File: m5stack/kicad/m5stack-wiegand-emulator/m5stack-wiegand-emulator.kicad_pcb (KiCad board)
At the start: 2 copper layers, 50 x 50 mm, 59 parts, among them J1 2x15 socket header, J2 2x15 pin header, J3 1x5 female, T1 TestPoint, T2 TestPoint, T3 TestPoint, T4 TestPoint, U1 RP2040, U2 ISOW7841, U3 SN74LVC2G126-EP, U5 SN74AHCT1G125, U6 FISM 1769405241

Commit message: M5: added solder jumpers for TC/RX
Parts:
- added JP4: Jumper:SolderJumper_2_Open, Jumper:SolderJumper-2_P1.3mm_Open_RoundedPad1.0x1.5mm, B.Cu at (114.9, 74.2)
- added JP5: Jumper:SolderJumper_2_Open, Jumper:SolderJumper-2_P1.3mm_Open_RoundedPad1.0x1.5mm, B.Cu at (114.9, 77.7)
- added JP8: Jumper:SolderJumper_2_Open, Jumper:SolderJumper-2_P1.3mm_Open_RoundedPad1.0x1.5mm, B.Cu at (114.9, 81.3)
- added JP9: Jumper:SolderJumper_2_Open, Jumper:SolderJumper-2_P1.3mm_Open_RoundedPad1.0x1.5mm, B.Cu at (114.9, 84.8)
- moved R14 47.1 mm to (108.0, 73.7)
- moved R15 47.1 mm to (108.0, 77.5)
- moved R16 47.1 mm to (108.0, 81.3)
- moved R19 47.1 mm to (108.0, 85.1)
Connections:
- R1 pad 2: /RXD2 -> Net-(JP8-B)
- R17 pad 2: /RXD1 -> Net-(JP4-B)
- R18 pad 2: /TXD1 -> Net-(JP5-B)
- R2 pad 2: /TXD2 -> Net-(JP9-B)
- U1 pad 18: /TXD2 -> Net-(JP9-B)
- U1 pad 19: /RXD2 -> Net-(JP8-B)
- U1 pad 22: /TXD1 -> Net-(JP5-B)
- U1 pad 23: /RXD1 -> Net-(JP4-B)

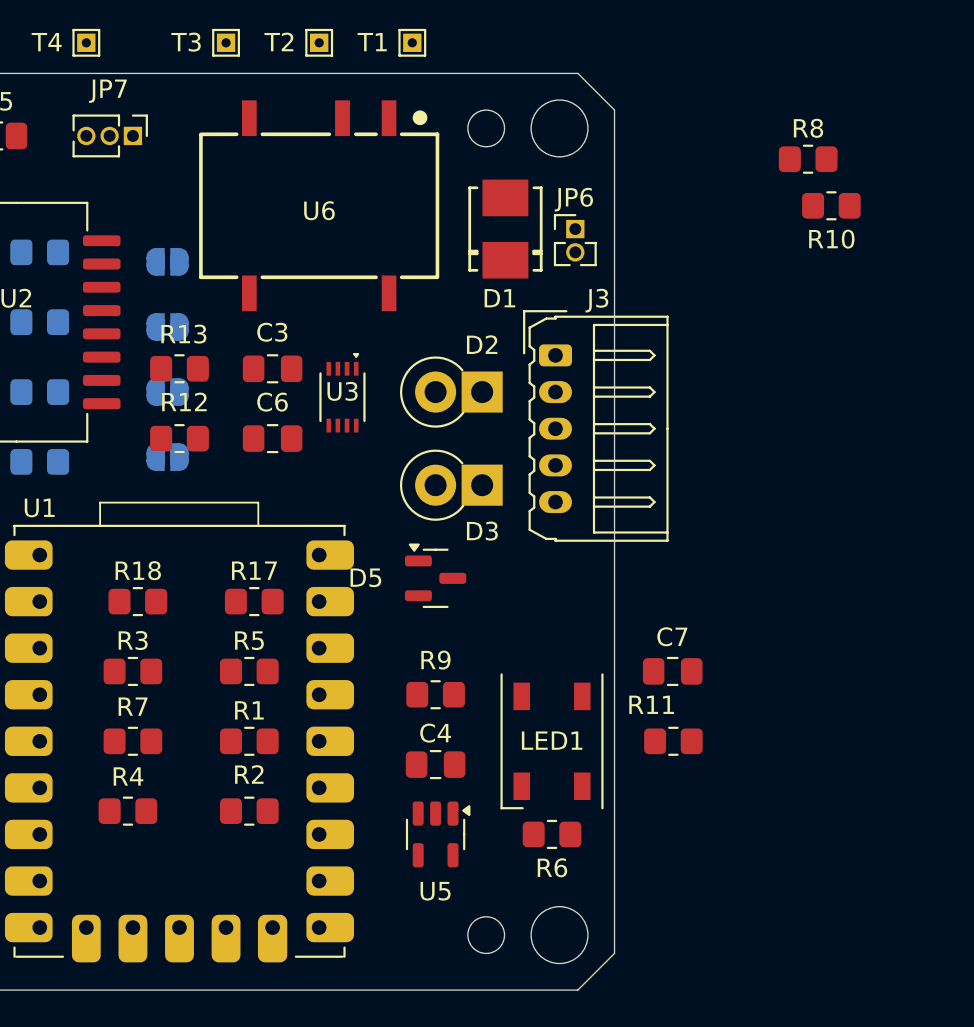
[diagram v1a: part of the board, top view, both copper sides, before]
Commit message: M5: replaced WS2812 driver with output from ISOW7843
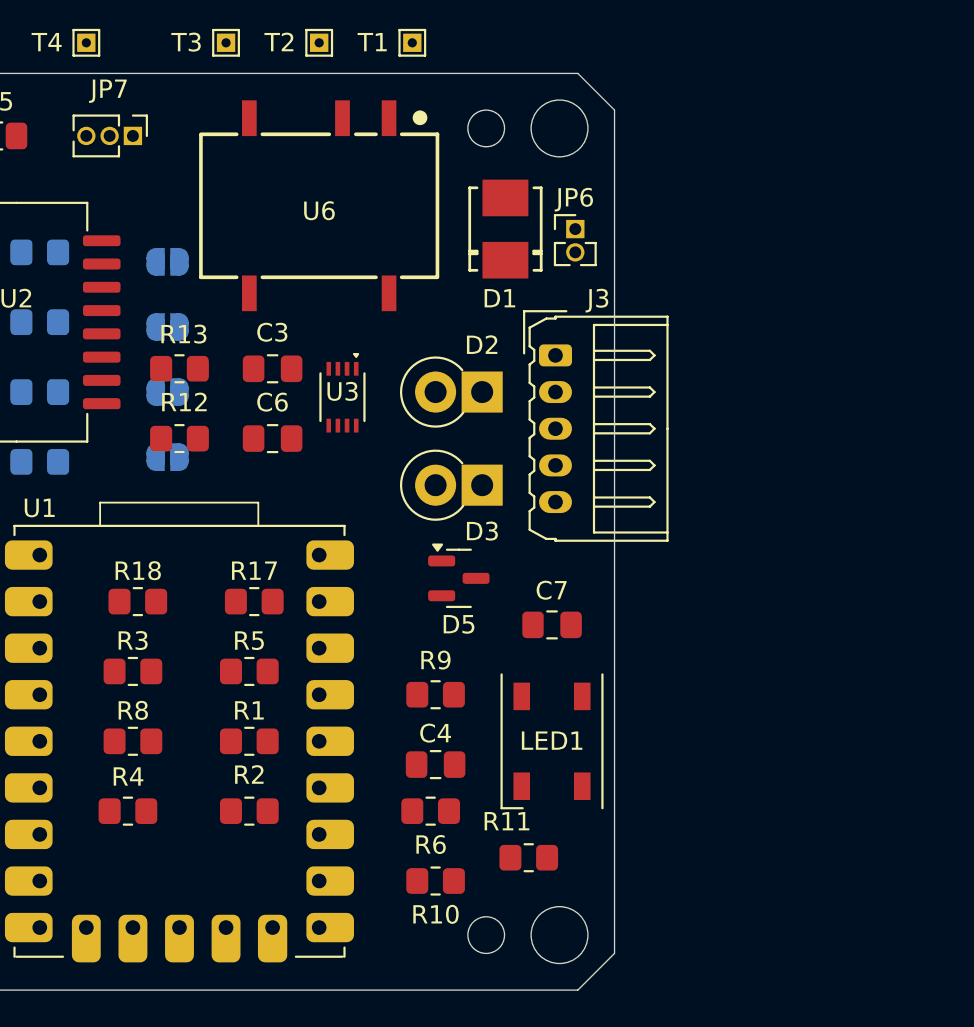
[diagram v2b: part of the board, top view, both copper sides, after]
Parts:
- removed R7: 10k, Resistor_SMD:R_0805_2012Metric_Pad1.20x1.40mm_HandSolder
- removed U5: SN74AHCT1G125, Package_TO_SOT_SMD:SOT-23-5
- moved R8 48.6 mm to (113.0, 100.3)
- moved R10 42.7 mm to (129.5, 108.0)
- moved R11 10.1 mm to (134.6, 106.7)
- moved C7 7.06 mm to (135.9, 94.0)
- moved R6 6.74 mm to (129.3, 104.1)
- moved D5 1.27 mm to (130.8, 91.4)
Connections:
- LED1 pad 1: +5V -> VISO
- R5 pad 2: Net-(U1-GP6) -> Net-(U1-GP13)
- R6 pad 1: Net-(U5-Y) -> Net-(U2-OUTC)
- R9 pad 1: Net-(U2-OUTC) -> VISO
- R9 pad 2: GND -> Net-(U3-1OE)
- U1 pad 10: unconnected-(U1-GP13-Pad10) -> Net-(U1-GP13)
- U1 pad 13: Net-(U1-GP10) -> unconnected-(U1-GP10-Pad13)
- U1 pad 17: Net-(U1-GP6) -> unconnected-(U1-GP6-Pad17)
- U2 pad 5: Net-(U1-GP10) -> Net-(U1-GP13)
- U3 pad 1: Net-(U2-OUTC) -> Net-(U3-1OE)
- U3 pad 7: Net-(U2-OUTC) -> Net-(U3-1OE)

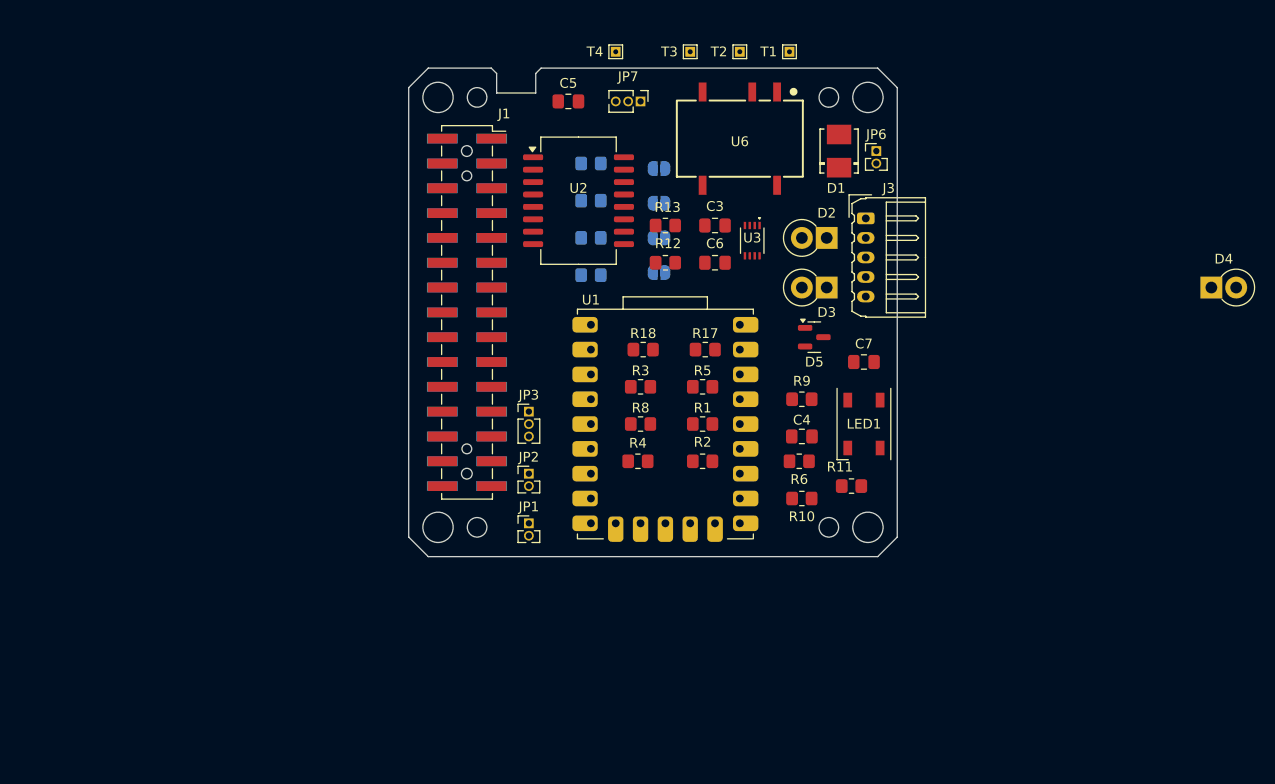
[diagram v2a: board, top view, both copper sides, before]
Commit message: M5: replaced THT TranzOrbs with SMD
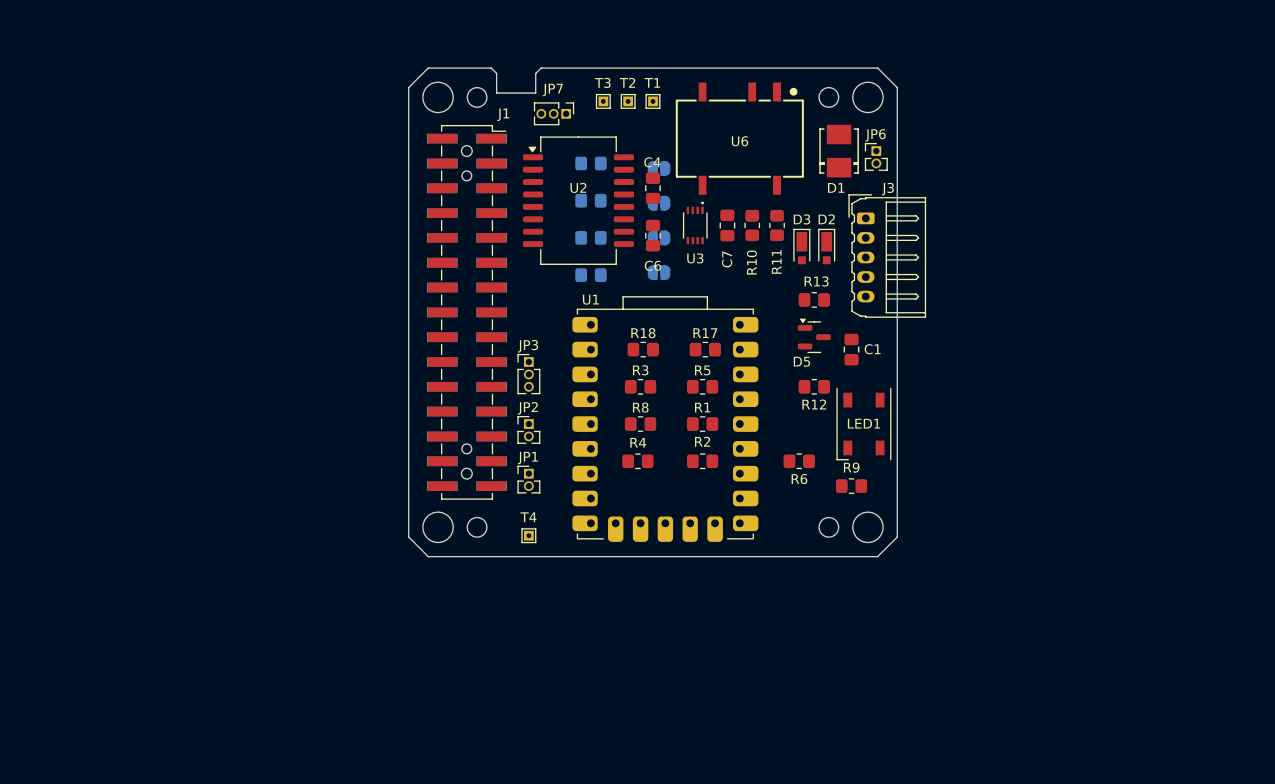
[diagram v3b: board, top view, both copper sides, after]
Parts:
- removed C3: 10nF, Capacitor_SMD:C_0805_2012Metric_Pad1.18x1.45mm_HandSolder
- removed C5: 0.1uF, Capacitor_SMD:C_0805_2012Metric_Pad1.18x1.45mm_HandSolder
- removed D4: SA5.0A, Diode_THT:D_DO-15_P2.54mm_Vertical_KathodeUp
- added C1: 10nF, Capacitor_SMD:C_0805_2012Metric_Pad1.18x1.45mm_HandSolder, F.Cu at (134.6, 92.7)
- D2, D3: value SA5.0A -> MSP5.0A; footprint Diode_THT:D_DO-15_P2.54mm_Vertical_KathodeUp -> Diode_SMD:D_MicroSMP_AK
- moved T4 50.3 mm to (101.6, 111.8)
- moved C4 29.6 mm to (114.3, 76.2), turned to -90 degrees
- moved R10 28.4 mm to (124.5, 80.0), turned to 90 degrees
- moved R11 27.7 mm to (127.0, 80.0), turned to 90 degrees
- moved R12 19.8 mm to (130.8, 96.5)
- moved C7 19.8 mm to (121.9, 80.0), turned to -90 degrees
- moved R13 17.0 mm to (130.8, 87.6)
- moved T1 14.9 mm to (114.3, 67.3)
- moved T2 12.5 mm to (111.8, 67.3)
- moved R9 10.2 mm to (134.6, 106.7)
- moved T3 10.2 mm to (109.2, 67.3)
- moved JP7 7.73 mm to (105.4, 68.6)
- moved C6 6.93 mm to (114.3, 81.0), turned to -90 degrees
- moved U3 6.03 mm to (118.6, 80.0)
- moved JP1 5.08 mm to (101.6, 105.4)
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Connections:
- C4 pad 1: +5V -> +3V3

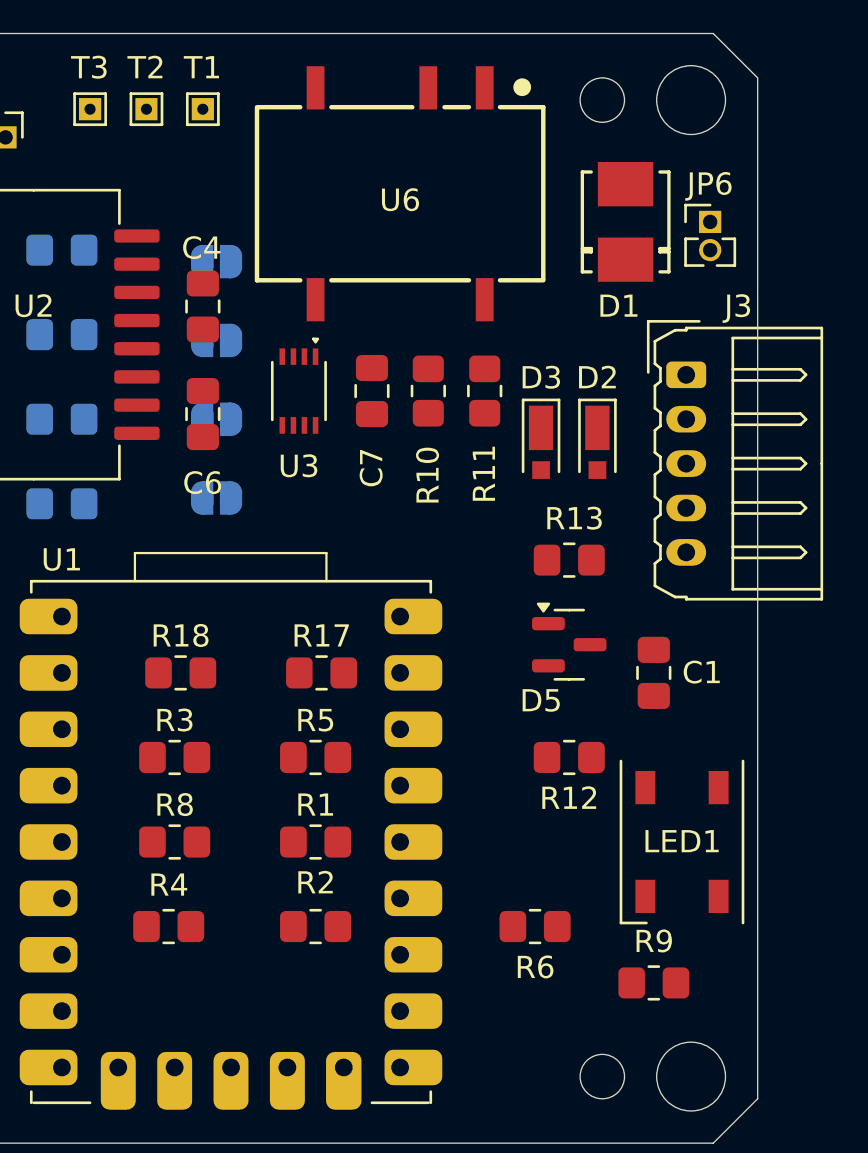
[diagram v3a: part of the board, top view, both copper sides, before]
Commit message: M5: reworked PCB footprints for overlap
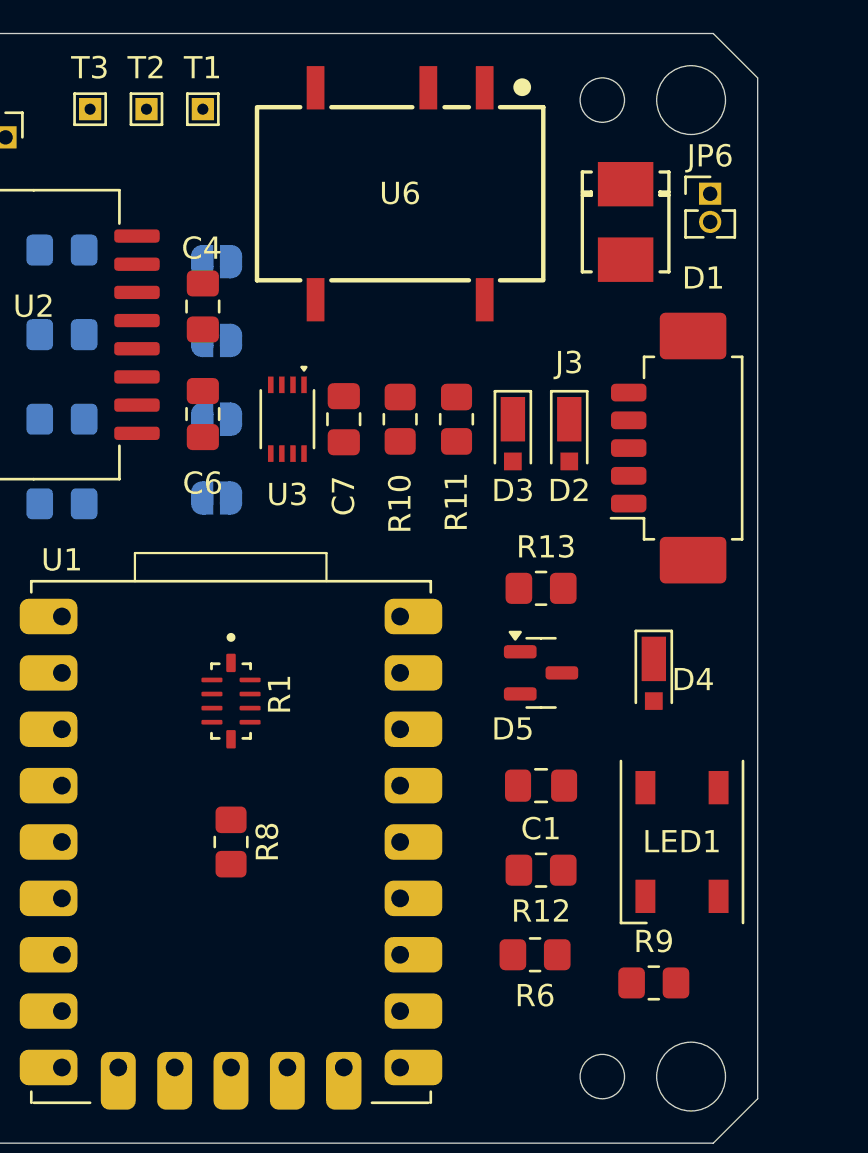
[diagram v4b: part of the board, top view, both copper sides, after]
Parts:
- removed R17, R18, R2, R3, R4, R5: 10k, Resistor_SMD:R_0805_2012Metric_Pad1.20x1.40mm_HandSolder
- removed REF** (x2): M5 Stack 1mm reference hole, uhppoted:M5 Stack 1mm reference hole
- removed REF**: M5 Stack 1.1mm reference hole, uhppoted:M5 Stack 1.1mm reference hole
- added D4: MSP5.0A, Diode_SMD:D_MicroSMP_AK, F.Cu at (134.6, 93.0)
- added M10: M5 Stack 1mm reference hole, uhppoted:M5 Stack 1mm reference hole, F.Cu at (95.2, 74.9)
- added M11: M5 Stack 1mm reference hole, uhppoted:M5 Stack 1mm reference hole, F.Cu at (95.2, 102.9)
- added M9: M5 Stack 1.1mm reference hole, uhppoted:M5 Stack 1.1mm reference hole, F.Cu at (95.2, 72.4)
- J3: footprint Connector_Molex:Molex_Micro-Latch_53254-0570_1x05_P2.00mm_Horizontal -> Connector_Molex:Molex_PicoBlade_53261-0571_1x05-1MP_P1.25mm_Horizontal
- R1: footprint Resistor_SMD:R_0805_2012Metric_Pad1.20x1.40mm_HandSolder -> uhppoted:RESCAV63P320X160X65-10N
- moved R1 7.41 mm to (115.6, 94.0), turned to -90 degrees
- moved C1 7.18 mm to (129.5, 97.8), turned to 0 degrees
- moved R12 5.24 mm to (129.5, 101.6)
- moved J3 3.31 mm to (135.9, 82.6), turned to 90 degrees
- moved R8 2.54 mm to (115.6, 100.3), turned to -90 degrees
- moved R13 1.80 mm to (129.5, 88.9)
- moved D5 1.80 mm to (129.5, 92.7)
- moved C7 1.80 mm to (120.7, 81.3)
- moved R10 1.80 mm to (123.2, 81.3)
- moved R11 1.80 mm to (125.7, 81.3)
- moved U3 1.37 mm to (118.1, 81.3)
- moved D2 1.33 mm to (130.8, 82.2)
- moved D3 1.33 mm to (128.3, 82.2)
- moved JP6 1.27 mm to (137.2, 71.1)
- moved R6 1.27 mm to (129.3, 105.4)
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- renumbered REF** to M1, REF** to M12, REF** to M2, REF** to M3, REF** to M4, REF** to M5, REF** to M6, REF** to M7, REF** to M8
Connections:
- R1 pad 1: +3V3 -> unconnected-(R1A-NC-Pad1)
- R1 pad 2: Net-(JP8-B) -> Net-(JP4-B)
- U1 pad 10: Net-(U1-GP13) -> Net-(R1G-R7.2)
- U1 pad 8: Net-(U1-GP15) -> Net-(R1E-R5.2)
- U1 pad 9: Net-(U1-GP14) -> Net-(R1F-R6.2)
- U2 pad 3: Net-(U1-GP15) -> Net-(R1E-R5.2)
- U2 pad 4: Net-(U1-GP14) -> Net-(R1F-R6.2)
- U2 pad 5: Net-(U1-GP13) -> Net-(R1G-R7.2)

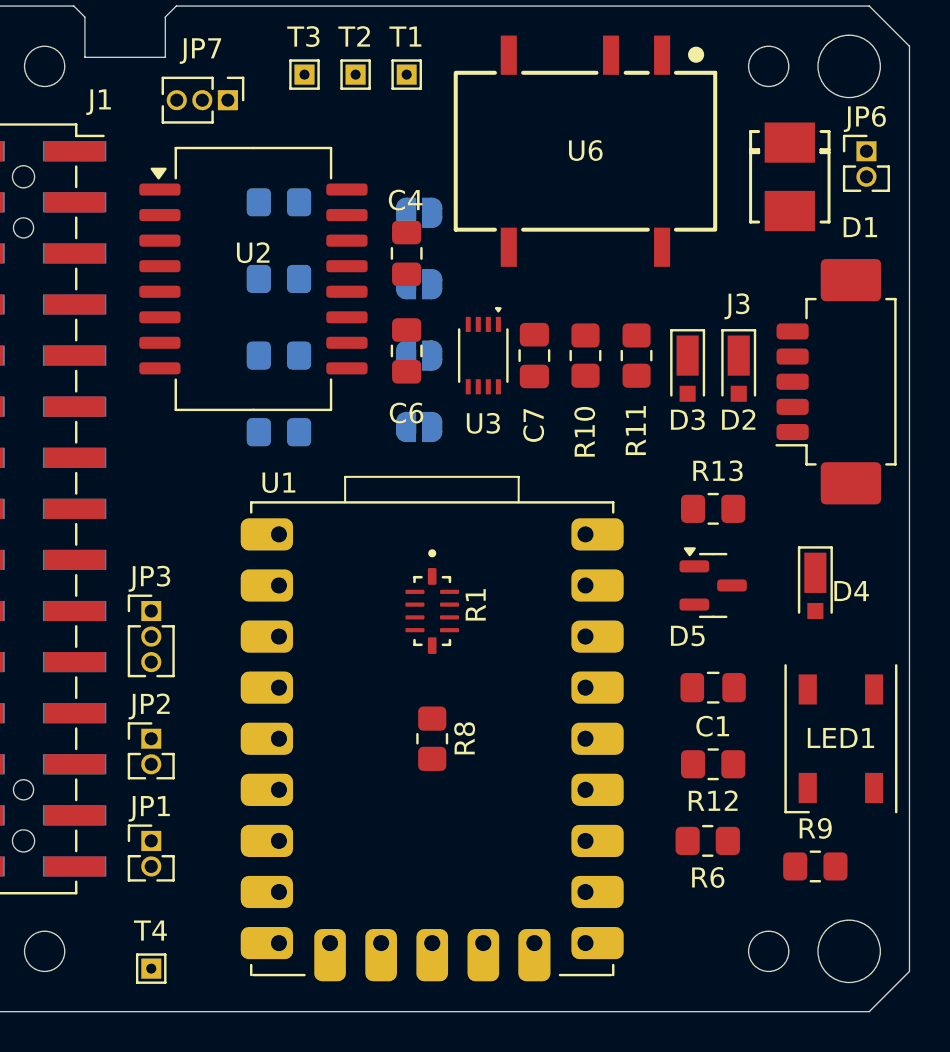
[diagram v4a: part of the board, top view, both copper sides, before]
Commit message: M5: added fiducial marks and logo/revision
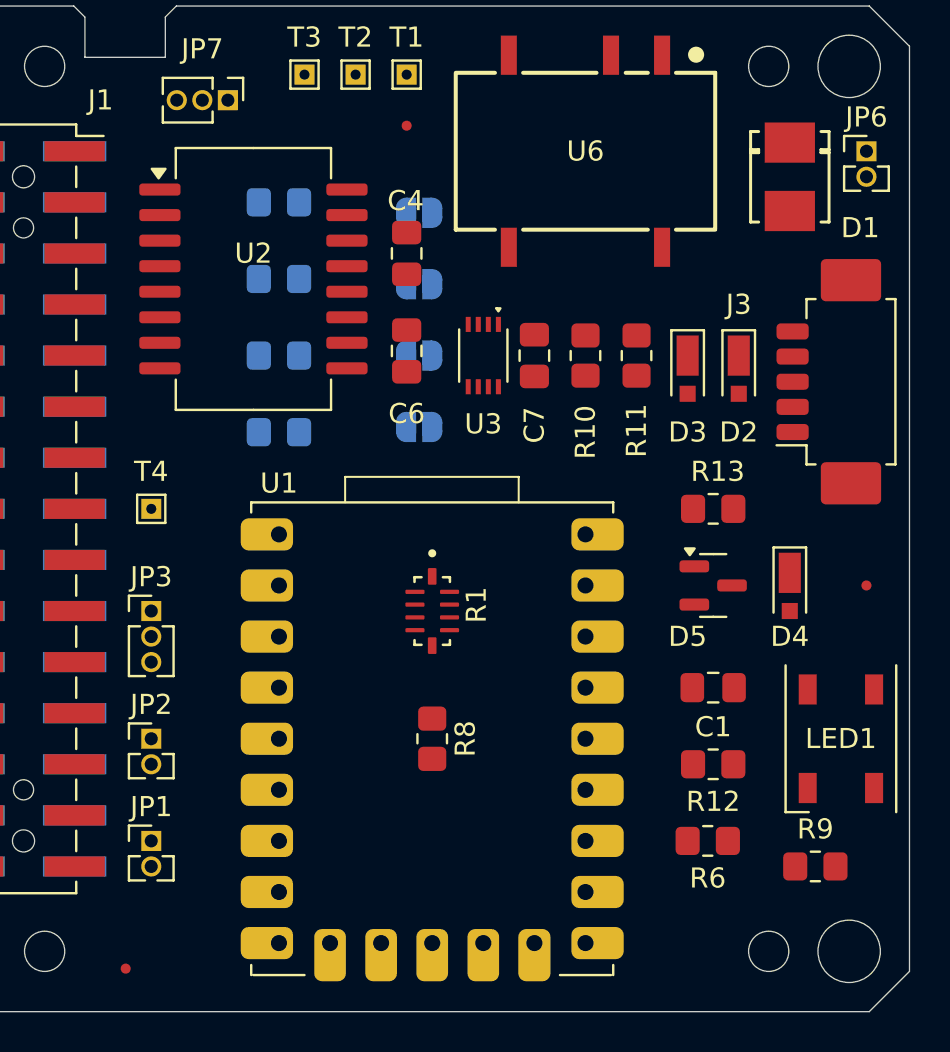
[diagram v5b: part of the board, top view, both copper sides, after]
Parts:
- removed M10, M11: M5 Stack 1mm reference hole, uhppoted:M5 Stack 1mm reference hole
- added F1: Fiducial_0.5mm_Mask1.5mm, Fiducial:Fiducial_0.5mm_Mask1.5mm, F.Cu at (114.3, 69.8)
- added F2: Fiducial_0.5mm_Mask1.5mm, Fiducial:Fiducial_0.5mm_Mask1.5mm, F.Cu at (100.3, 111.8)
- added F3: Fiducial_0.5mm_Mask1.5mm, Fiducial:Fiducial_0.5mm_Mask1.5mm, F.Cu at (137.2, 92.7)
- added G***: LOGO, uhppoted:LOGO, B.Cu at (133.3, 76.2)
- added REF**: M5 Stack 1mm reference hole, uhppoted:M5 Stack 1mm reference hole, F.Cu at (95.2, 74.9)
- added REF**: M5 Stack 1mm reference hole, uhppoted:M5 Stack 1mm reference hole, F.Cu at (95.2, 102.9)
- D2, D3, D4: footprint Diode_SMD:D_MicroSMP_AK -> uhppoted:MSP5.0A
- R1: footprint uhppoted:RESCAV63P320X160X65-10N -> uhppoted:EXB-D10C103J
- moved T4 22.9 mm to (101.6, 88.9)
- moved D4 1.27 mm to (133.3, 93.0)
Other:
- board text added: "WIEGAND EMULATOR Rev.0"
